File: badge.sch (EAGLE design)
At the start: 177 parts, among them CN4 MicroUSB, IC3 MEGA8-AI, Q1 BSS138, Q2 BSS138, T1 MMUN2133LT1G, U1 TPS61090RSAR, U2 MCP73871, U3 LIS3DHTR, U4 MIC5225-3.3, Y1 16.00MHz

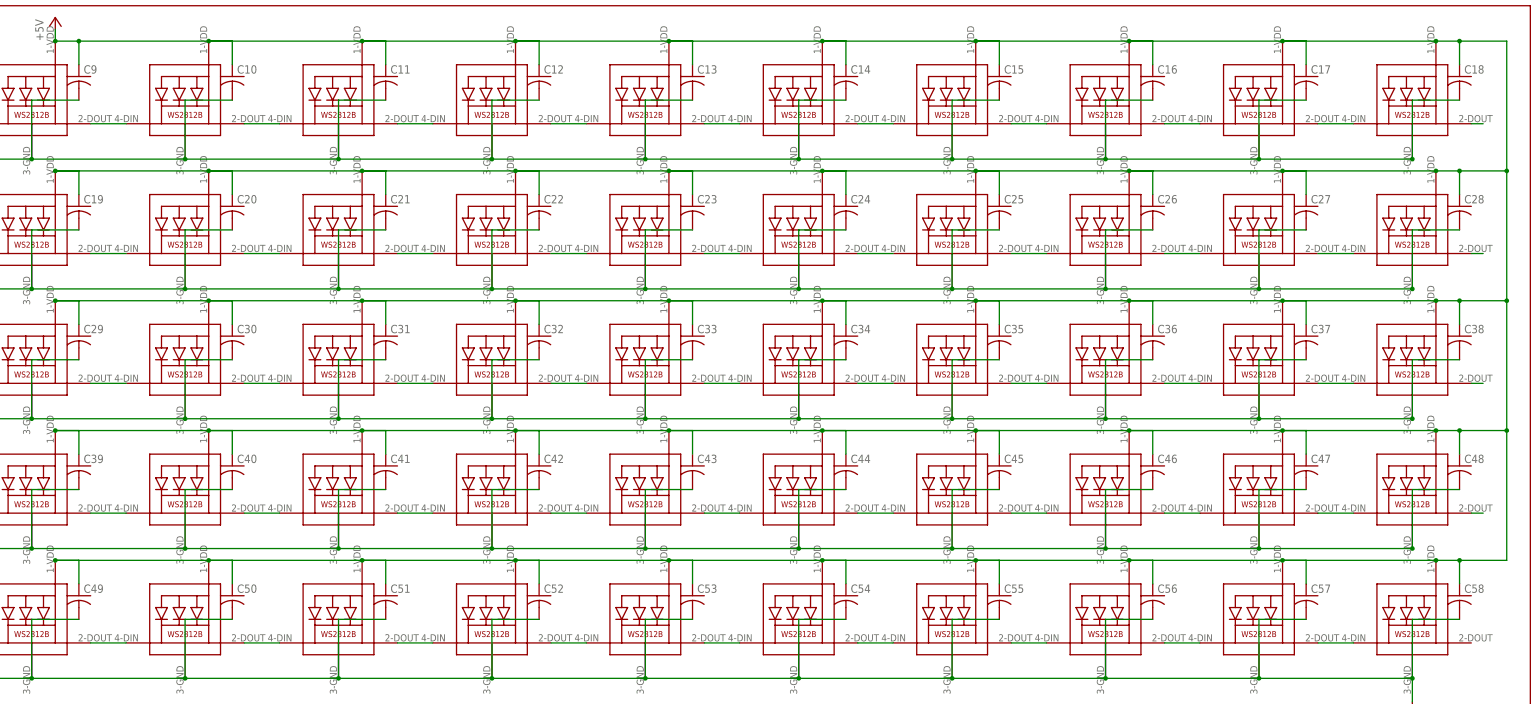
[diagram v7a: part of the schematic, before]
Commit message: generated a BOM and started to add parts to it on digikey
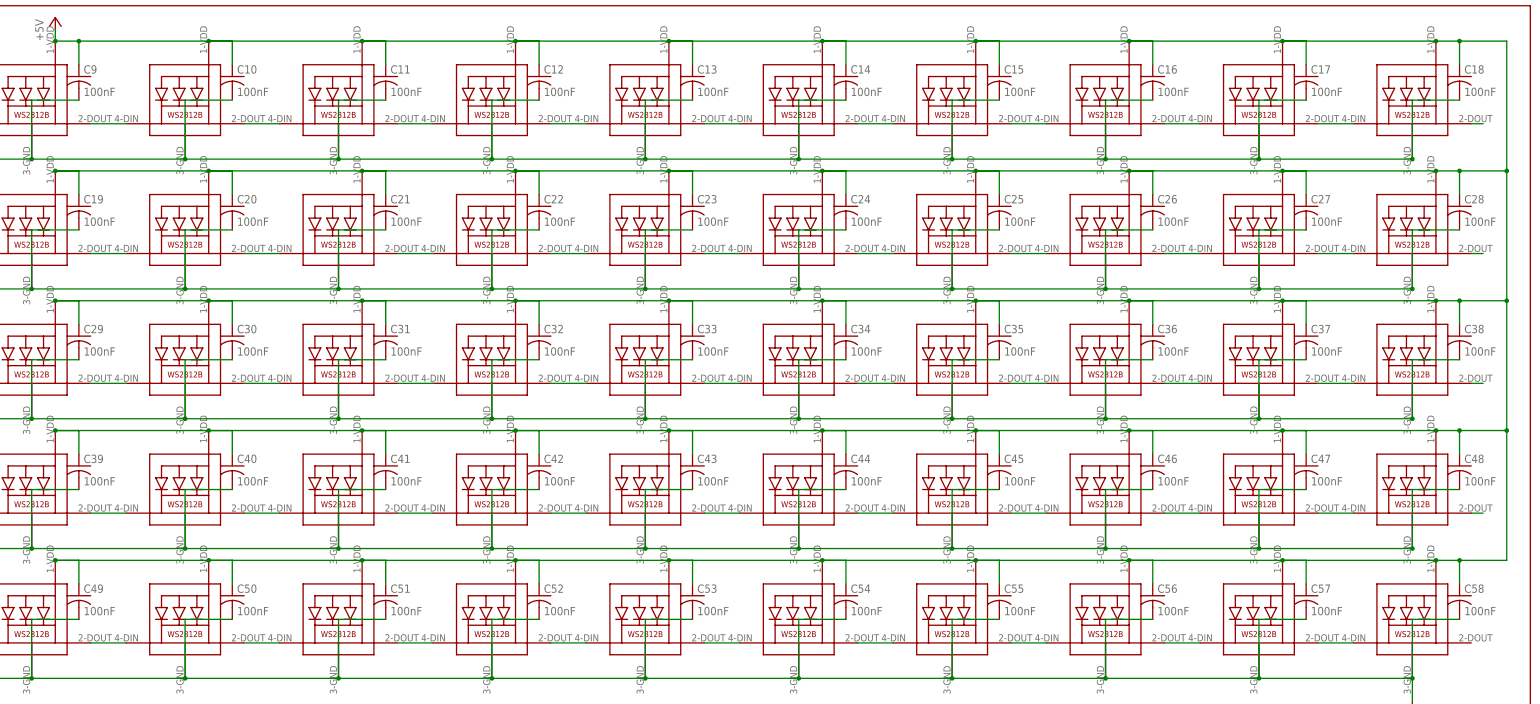
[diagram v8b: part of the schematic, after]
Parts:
- C10, C11, C12, C13, C14, C15, C16, C17, C18, C19, C20, C21, C22, C23, C24, C25, C26, C27, C28, C29, C30, C31, C32, C33, C34, C35, C36, C37, C38, C39, C40, C41, C42, C43, C44, C45, C46, C47, C48, C49, C50, C51, C52, C53, C54, C55, C56, C57, C58, C9: value (none) -> 100nF
